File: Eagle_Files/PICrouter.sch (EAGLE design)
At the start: 80 parts, among them IC1 PIC32MX675F512H, IC2 48M033F, IC3 DP83848, J3 POWER_JACK, Q1 20MHz, Q2 BSS84, U1 DEVICE, X1 USB-A-H

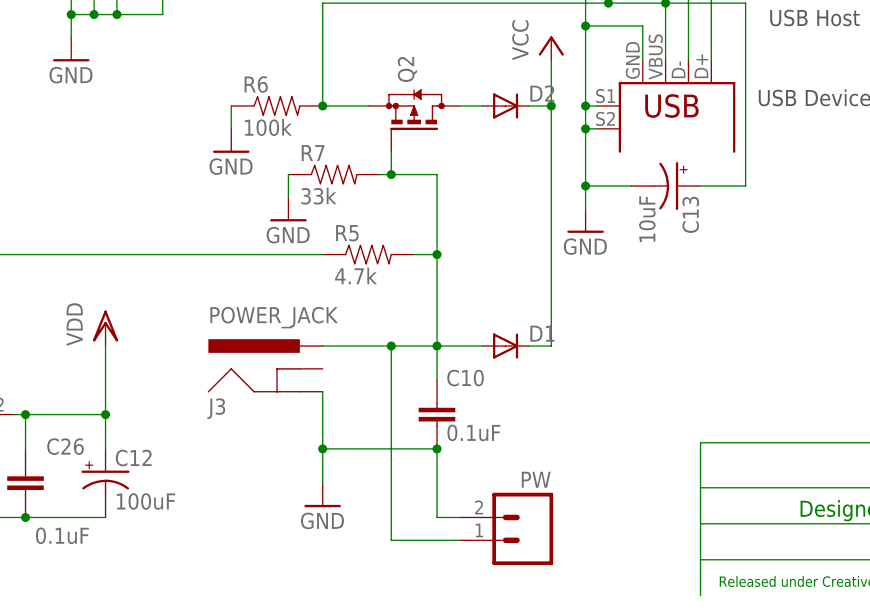
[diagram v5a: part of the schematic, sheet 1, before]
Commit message: Released PICrouter schematic and board v0.9.
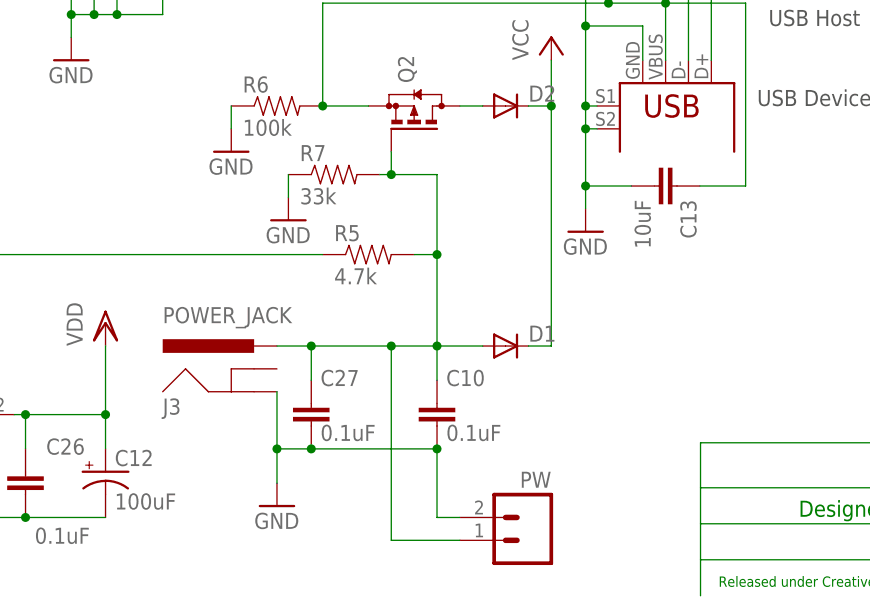
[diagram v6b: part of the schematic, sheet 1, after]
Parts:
- added C27: 0.1uF, rcl:C-EUC2012
- C13: device rcl:CPOL-USC -> rcl:C-EUC2012
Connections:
- net GND: now also C13.2, C27.2; no longer C13.-
- net N$46: now also C27.1
- net N$50: now also C13.1; no longer C13.+
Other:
- moved on the sheet: J3
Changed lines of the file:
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@@
 <setting verticaltext="up"/>
 </settings>
-<grid distance="0.1" unitdist="inch" unit="inch" style="lines" multiple="1" display="no" altdistance="0.01" altunitdist="inch" altunit="inch"/>
+<grid distance="0.05" unitdist="inch" unit="inch" style="lines" multiple="1" display="no" altdistance="0.01" altunitdist="inch" altunit="inch"/>
 <layers>
 <layer number="1" name="Top" color="4" fill="1" visible="no" active="no"/>
@@
 <part name="GND2" library="supply1" deviceset="GND" device=""/>
 <part name="GND6" library="supply1" deviceset="GND" device=""/>
-<part name="C13" library="rcl" deviceset="CPOL-US" device="C" value="10uF"/>
+<part name="C13" library="rcl" deviceset="C-EU" device="C2012" value="10uF"/>
 <part name="GND10" library="supply1" deviceset="GND" device=""/>
 <part name="D1" library="diode" deviceset="DIODE-" device="SOD123"/>
@@
 <part name="GND29" library="supply1" deviceset="GND" device=""/>
 <part name="C26" library="rcl" deviceset="C-EU" device="C2012" value="0.1uF"/>
+<part name="C27" library="rcl" deviceset="C-EU" device="C2012" value="0.1uF"/>
 </parts>
 <sheets>
@@
 <instance part="GND6" gate="1" x="189.23" y="44.45"/>
 <instance part="C13" gate="G$1" x="199.39" y="49.53" rot="R270"/>
-<instance part="GND10" gate="1" x="160.02" y="13.97"/>
+<instance part="GND10" gate="1" x="154.94" y="13.97"/>
 <instance part="D1" gate="G$1" x="180.34" y="31.75"/>
 <instance part="D2" gate="G$1" x="180.34" y="58.42"/>
@@
 <instance part="C9" gate="G$1" x="207.01" y="133.35"/>
 <instance part="GND19" gate="1" x="212.09" y="138.43" rot="R90"/>
-<instance part="J3" gate="G$1" x="157.48" y="24.13"/>
+<instance part="J3" gate="G$1" x="152.4" y="24.13"/>
 <instance part="U1" gate="G$1" x="195.58" y="60.96" rot="R270"/>
 <instance part="X1" gate="G$1" x="214.63" y="76.2" smashed="yes" rot="MR270"/>
@@
 <attribute name="VALUE" x="128.016" y="9.779" size="1.778" layer="96"/>
 </instance>
+<instance part="C27" gate="G$1" x="158.75" y="25.4" smashed="yes">
+<attribute name="NAME" x="159.766" y="27.305" size="1.778" layer="95"/>
+<attribute name="VALUE" x="159.766" y="21.209" size="1.778" layer="96"/>
+</instance>
 </instances>
 <busses>
@@
 <junction x="189.23" y="49.53"/>
 <pinref part="GND6" gate="1" pin="GND"/>
-<pinref part="C13" gate="G$1" pin="-"/>
+<pinref part="C13" gate="G$1" pin="2"/>
 <pinref part="U1" gate="G$1" pin="GND"/>
 <wire x1="195.58" y1="63.5" x2="195.58" y2="67.31" width="0.1524" layer="91"/>
@@
 </segment>
 <segment>
-<wire x1="160.02" y1="20.32" x2="160.02" y2="16.51" width="0.1524" layer="91"/>
-<wire x1="172.72" y1="20.32" x2="160.02" y2="20.32" width="0.1524" layer="91"/>
+<wire x1="154.94" y1="20.32" x2="154.94" y2="16.51" width="0.1524" layer="91"/>
+<wire x1="172.72" y1="20.32" x2="158.75" y2="20.32" width="0.1524" layer="91"/>
+<wire x1="158.75" y1="20.32" x2="154.94" y2="20.32" width="0.1524" layer="91"/>
 <wire x1="175.26" y1="12.7" x2="172.72" y2="12.7" width="0.1524" layer="91"/>
 <wire x1="172.72" y1="12.7" x2="172.72" y2="20.32" width="0.1524" layer="91"/>
@@
 <pinref part="PW" gate="G$1" pin="2"/>
 <pinref part="J3" gate="G$1" pin="GND"/>
-<wire x1="160.02" y1="26.67" x2="160.02" y2="20.32" width="0.1524" layer="91"/>
-<junction x="160.02" y="20.32"/>
+<wire x1="154.94" y1="26.67" x2="154.94" y2="20.32" width="0.1524" layer="91"/>
+<junction x="154.94" y="20.32"/>
+<pinref part="C27" gate="G$1" pin="2"/>
+<junction x="158.75" y="20.32"/>
 </segment>
 <segment>
@@
 <pinref part="R5" gate="G$1" pin="2"/>
 <pinref part="J3" gate="G$1" pin="PWR"/>
-<wire x1="160.02" y1="31.75" x2="167.64" y2="31.75" width="0.1524" layer="91"/>
+<wire x1="154.94" y1="31.75" x2="158.75" y2="31.75" width="0.1524" layer="91"/>
 <junction x="167.64" y="31.75"/>
+<pinref part="C27" gate="G$1" pin="1"/>
+<wire x1="158.75" y1="31.75" x2="167.64" y2="31.75" width="0.1524" layer="91"/>
+<wire x1="158.75" y1="27.94" x2="158.75" y2="31.75" width="0.1524" layer="91"/>
+<junction x="158.75" y="31.75"/>
 </segment>
 </net>
@@
 <pinref part="Q2" gate="G$1" pin="S"/>
 <pinref part="R6" gate="G$1" pin="2"/>
-<pinref part="C13" gate="G$1" pin="+"/>
+<pinref part="C13" gate="G$1" pin="1"/>
 <pinref part="R4" gate="G$1" pin="1"/>
 <pinref part="C9" gate="G$1" pin="2"/>

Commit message: Released PICrouter schematic and board v0.91.
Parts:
- removed C25: 150uF, rcl:CPOL-USC
- removed C27: 0.1uF, rcl:C-EUC2012
- removed D1, D2: (no value), diode:DIODE-SOD123
- removed F1: PTCSMD, SparkFun:PTCSMD
- removed J3: POWER_JACK, SparkFun:POWER_JACKPTH_LOCK
- removed Q2: BSS84, transistor-small-signal:BSS84
- removed R7: 33k, SparkFun:RESISTOR0603-RES
- removed U1: DEVICE, SparkFun:USB+SHIELD
- removed X1: USB-A-H, SparkFun:USB-A-H
- added C28, C29, C31, C32: 0.1uF, rcl:C-EUC2012
- added C30: 10uF, rcl:C-EUC2012
- added F2: PTCSMD, SparkFun:PTCSMD
- added IC4: TPS2111A, SparkFun:TPS2111A
- added J1: POWER_JACK, SparkFun:POWER_JACKPTH_LOCK
- added R28: 400, SparkFun:RESISTOR0603-RES
- added U2: DEVICE, SparkFun:USB+SHIELD
- added X2: USB-A-H, SparkFun:USB-A-H
- C10: value 0.1uF -> 150uF; device rcl:C-EUC2012 -> rcl:CPOL-USC
- C13: value 10uF -> 150uF; device rcl:C-EUC2012 -> rcl:CPOL-USC
- R6: value 100k -> 10k
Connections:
- removed net N$45: IC1.D-/RG3, U1.D-, X1.D+
- removed net N$46: C10.1, C27.1, D1.A, J3.PWR, PW.1, Q2.G, R5.2, R7.2
- removed net N$5: IC1.D+/RG2, U1.D+, X1.D-
- removed net N$50: C13.1, C25.+, C9.2, F1.1, IC1.VBUS, Q2.S, R4.1, R6.2, U1.VBUS, X1.GND
- removed net N$60: D2.A, Q2.D
- new net D+: IC1.D+/RG2, U2.D+, X2.D-
- new net D-: IC1.D-/RG3, U2.D-, X2.D+
- new net N$61: IC4.ILIM, R28.2
- new net SELF: C29.1, C31.1, C32.1, IC4.D1, IC4.IN1, J1.PWR, PW.1, R5.2, R6.2
- new net VBUS: C28.1, C30.1, C9.2, IC1.VBUS, IC4.IN2, R4.1, U2.VBUS
- new net VBUS_HOST: C10.+, F2.2, X2.GND
- net GND: now also C10.-, C13.-, C28.2, C29.2, C30.2, C31.2, C32.2, IC4.D0, IC4.GND, IC4.VSNS, J1.GND, R28.1, U2.GND, U2.P$1, U2.P$2, X2.S1, X2.S2, X2.VBUS; no longer C10.2, C13.2, C25.-, C27.2, J3.GND, R7.1, U1.GND, U1.P$1, U1.P$2, X1.S1, X1.S2, X1.VBUS
- net VCC: now also C13.+, F2.1, IC4.OUT; no longer D1.C, D2.C, F1.2
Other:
- note added: "04/10/2012"
- note added: "PICrouter v0.91"
- note removed: "03/29/2012"
- note removed: "PICrouter v0.7"

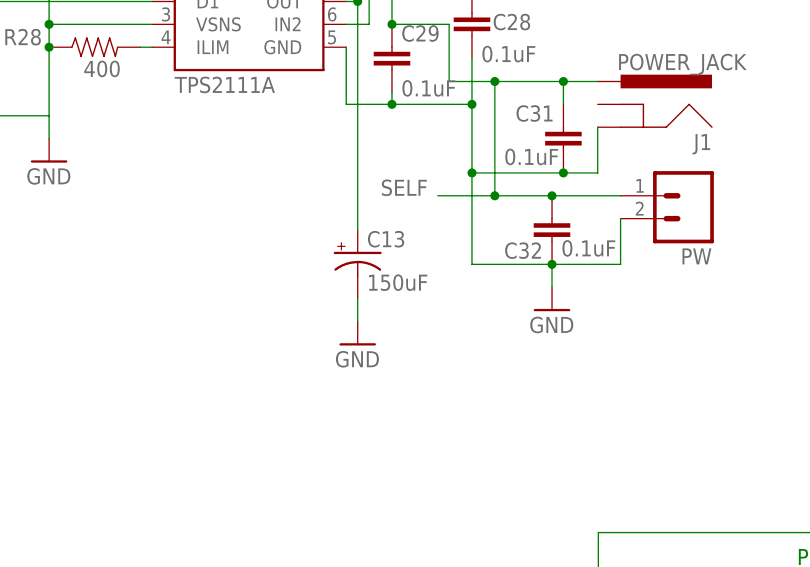
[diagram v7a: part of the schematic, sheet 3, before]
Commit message: Released PICrouter schematic and board v0.92.
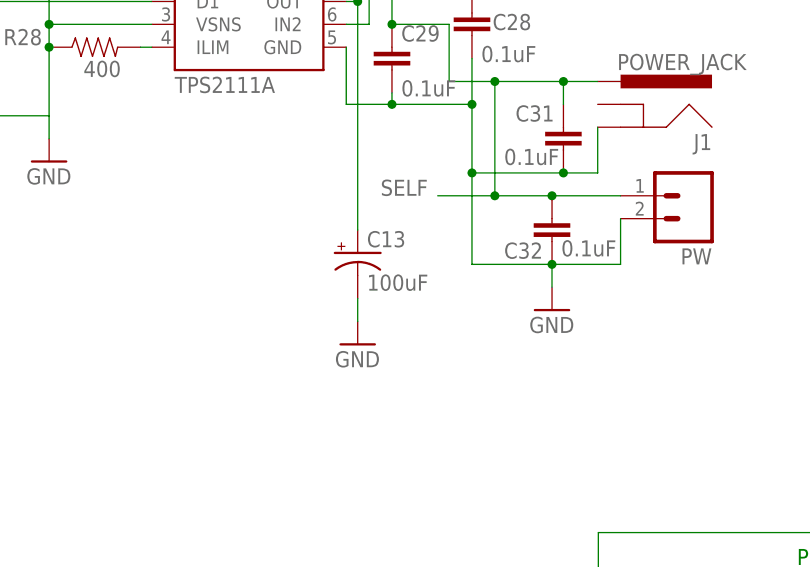
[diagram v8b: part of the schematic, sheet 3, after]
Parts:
- C13: value 150uF -> 100uF
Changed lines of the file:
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@@
 <part name="GND6" library="supply1" deviceset="GND" device=""/>
 <part name="R6" library="SparkFun" deviceset="RESISTOR" device="0603-RES" value="10k"/>
-<part name="C13" library="rcl" deviceset="CPOL-US" device="C" value="150uF"/>
+<part name="C13" library="rcl" deviceset="CPOL-US" device="C" value="100uF"/>
 <part name="GND10" library="supply1" deviceset="GND" device=""/>
 </parts>
